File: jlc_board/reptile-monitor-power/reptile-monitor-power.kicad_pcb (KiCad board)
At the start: 4 copper layers, 38.1 x 53.3 mm, 14 parts, among them J1 AC_IN, J2 LOAD_2, J3 LOAD_1, J4 POWER CONN, K1 ALDP105W, K2 ALDP105W, U1 NUD3105DMT1G

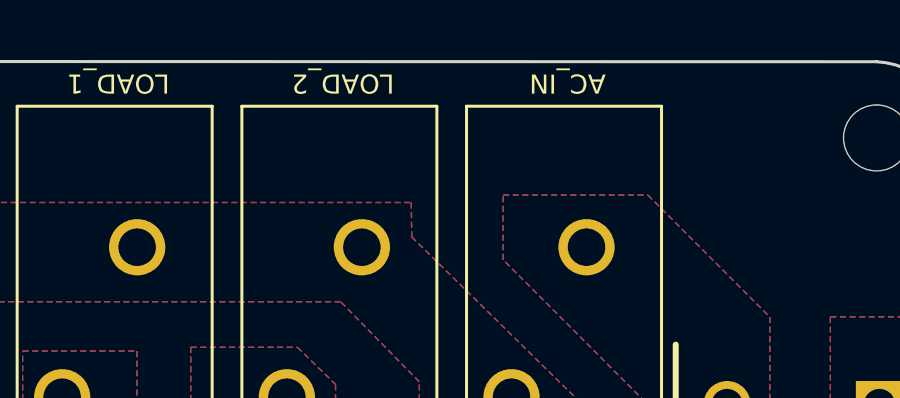
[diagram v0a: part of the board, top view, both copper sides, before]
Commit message: consolidate kicad libraries
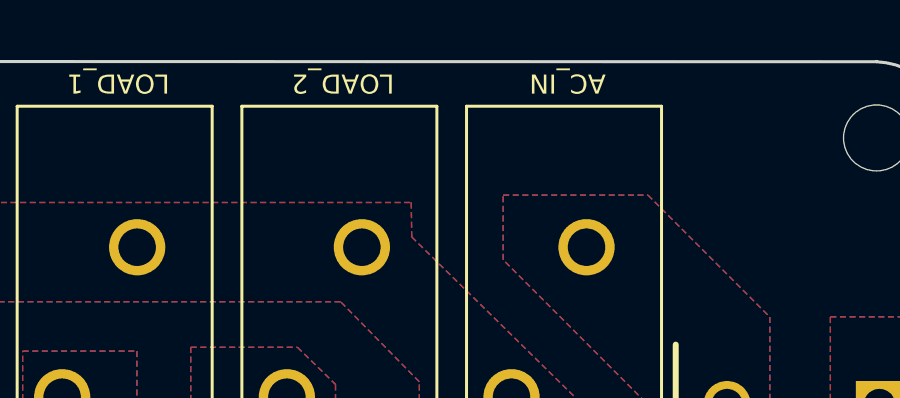
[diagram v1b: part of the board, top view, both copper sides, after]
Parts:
- F1: footprint SamacSys_Parts:TO508P400X850X850-2P -> reptile-monitor-power1:TO508P400X850X850-2P
- J1, J2, J3: footprint SamacSys_Parts:128340212 -> reptile-monitor-power1:TE Connectivity PC Terminal Block 128340212
- J4: footprint Connector_PinHeader_2.54mm:PinHeader_1x04_P2.54mm_Vertical -> reptile-monitor-power1:PinHeader_1x04_P2.54mm_Vertical
- PS1: footprint Converter_ACDC:Converter_ACDC_HiLink_HLK-PMxx -> reptile-monitor-power1:Converter_ACDC_HiLink_HLK-PMxx
- RV1: footprint Varistor:RV_Disc_D7mm_W3.4mm_P5mm -> reptile-monitor-power1:RV_Disc_D7mm_W3.4mm_P5mm
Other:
- board text added: "Rev. 3, July 2021"
- board text removed: "Rev. 3 June 2021"

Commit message: rev4
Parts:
- added REF**: WAFFLE, reptile-monitor:LOGO, B.Cu at (152.7, 83.9)
- J1, J2, J3: footprint reptile-monitor-power1:TE Connectivity PC Terminal Block 128340212 -> reptile-monitor-power:TE Connectivity PC Terminal Block 128340212
- RV1: footprint reptile-monitor-power1:RV_Disc_D7mm_W3.4mm_P5mm -> reptile-monitor-power:RV_Disc_D7mm_W3.4mm_P5mm
- moved F1 4.90 mm to (158.3, 59.9), turned to 90 degrees
- moved J1 2.60 mm to (152.9, 54.4)
- moved K1 2.60 mm to (137.5, 81.8)
- moved K2 2.60 mm to (129.2, 81.8)
- moved PS1 2.60 mm to (156.9, 64.5)
- moved J2 2.60 mm to (145.4, 54.4)
- moved J3 2.60 mm to (137.9, 54.4)
- moved RV1 1.84 mm to (132.3, 55.7)
- moved U1 1.40 mm to (138.8, 89.2)
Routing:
- net L1: track 22.2 -> 23.8 mm
- net RLY2: track 6.62 -> 8.09 mm
- net L2: track 23.9 -> 25.1 mm
- net RLY1: track 9.13 -> 10.3 mm
- net GND: track 1.97 -> 3.09 mm
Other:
- rule pad_to_mask_clearance: 0.0508 -> 0
- board text added: "+5V"
- board text added: "GND"
- board text added: "L1"
- board text added: "L2"
- board text added: "Rev. 4, Aug 2021"
- board text removed: "Rev. 3, July 2021"

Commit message: updates
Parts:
- F1: footprint reptile-monitor-power1:TO508P400X850X850-2P -> reptile-monitor-power:TO508P400X850X850-2P
- J4: footprint reptile-monitor-power1:PinHeader_1x04_P2.54mm_Vertical -> reptile-monitor-power:PinHeader_1x04_P2.54mm_Vertical
- PS1: footprint reptile-monitor-power1:Converter_ACDC_HiLink_HLK-PMxx -> reptile-monitor-power:Converter_ACDC_HiLink_HLK-PMxx
- moved REF1 58.5 mm to (129.4, 101.6), turned to 180 degrees
- moved REF1 58.5 mm to (129.4, 53.3), turned to 0 degrees
- moved REF1 58.4 mm to (162.5, 101.6), turned to 180 degrees
- moved REF1 58.4 mm to (162.5, 53.3), turned to 0 degrees
- moved RV1 51.5 mm to (159.7, 99.3), turned to 90 degrees
- moved J3 48.9 mm to (154.1, 100.6), turned to 0 degrees
- moved J4 48.9 mm to (139.5, 53.8)
- moved J1 48.2 mm to (139.1, 100.6), turned to 0 degrees
- moved J2 46.2 mm to (146.6, 100.6), turned to 0 degrees
- moved F1 42.8 mm to (133.7, 95.0), turned to -90 degrees
- moved K2 34.6 mm to (162.8, 73.2), turned to -90 degrees
- moved PS1 34.0 mm to (135.1, 90.5), turned to 90 degrees
- moved U1 27.5 mm to (153.2, 65.8), turned to 180 degrees
- moved K1 19.1 mm to (154.5, 73.2), turned to -90 degrees
- moved REF** 18.4 mm to (139.5, 71.1), turned to -90 degrees
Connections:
- J4 pad 1: +5V -> GND
- J4 pad 2: GND -> +5V
- J4 pad 3: L2 -> L1
- J4 pad 4: L1 -> L2
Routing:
- net L2: track 25.1 -> 16.6 mm
- net L1: track 23.8 -> 16.1 mm

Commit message: tt-relay
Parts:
- moved U1 6.17 mm to (155.5, 60.1), turned to 90 degrees
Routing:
- net RLY2: track 8.09 -> 18.0 mm
- net RLY1: track 10.3 -> 13.2 mm
- net L1: track 16.1 -> 13.7 mm
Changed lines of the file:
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@@
   )
   (footprint "reptile-monitor-power:ON_Semi-318F-0-0-0" (layer "F.Cu")
-    (at 153.2382 65.786 180)
+    (at 155.5242 60.0525 90)
     (property "Current - Output (Max)" "300mA")
     (property "Sheetfile" "reptile-monitor-power.kicad_sch")
@@
     (property "temperature range low" "-40°C")
     (property "voltage" "6V")
-    (fp_text reference "U1" (at -1.65 -2.4) (layer "F.SilkS") hide
-      (effects (font (size 1 1) (thickness 0.15)) (justify right))
+    (fp_text reference "U1" (at -1.65 -2.4 90) (layer "F.SilkS") hide
+      (effects (font (size 1 1) (thickness 0.15)) (justify left))
     )
-    (fp_text value "NUD3105DMT1G" (at 0 0) (layer "F.SilkS") hide
+    (fp_text value "NUD3105DMT1G" (at 0 0 90) (layer "F.SilkS") hide
       (effects (font (size 1.27 1.27) (thickness 0.15)))
     )
@@
     (fp_line (start -0.75 1.5) (end -0.75 -1.5) (layer "F.Fab") (width 0.15))
     (fp_line (start -0.75 -1.5) (end 0.75 -1.5) (layer "F.Fab") (width 0.15))
-    (pad "1" smd rect (at -1.2 -0.95 180) (size 1 0.7) (layers "F.Cu" "F.Paste" "F.Mask")
+    (pad "1" smd rect (at -1.2 -0.95 90) (size 1 0.7) (layers "F.Cu" "F.Paste" "F.Mask")
       (net 7 "GND") (pinfunction "1_Source") (pintype "unspecified"))
-    (pad "2" smd rect (at -1.2 0 180) (size 1 0.7) (layers "F.Cu" "F.Paste" "F.Mask")
+    (pad "2" smd rect (at -1.2 0 90) (size 1 0.7) (layers "F.Cu" "F.Paste" "F.Mask")
       (net 5 "L2") (pinfunction "1_Gate") (pintype "unspecified"))
-    (pad "3" smd rect (at -1.2 0.95 180) (size 1 0.7) (layers "F.Cu" "F.Paste" "F.Mask")
+    (pad "3" smd rect (at -1.2 0.95 90) (size 1 0.7) (layers "F.Cu" "F.Paste" "F.Mask")
       (net 2 "RLY1") (pinfunction "2_Drain") (pintype "unspecified"))
-    (pad "4" smd rect (at 1.2 0.95 180) (size 1 0.7) (layers "F.Cu" "F.Paste" "F.Mask")
+    (pad "4" smd rect (at 1.2 0.95 90) (size 1 0.7) (layers "F.Cu" "F.Paste" "F.Mask")
       (net 7 "GND") (pinfunction "2_Source") (pintype "unspecified"))
-    (pad "5" smd rect (at 1.2 0 180) (size 1 0.7) (layers "F.Cu" "F.Paste" "F.Mask")
+    (pad "5" smd rect (at 1.2 0 90) (size 1 0.7) (layers "F.Cu" "F.Paste" "F.Mask")
       (net 6 "L1") (pinfunction "2_Gate") (pintype "unspecified"))
-    (pad "6" smd rect (at 1.2 -0.95 180) (size 1 0.7) (layers "F.Cu" "F.Paste" "F.Mask")
+    (pad "6" smd rect (at 1.2 -0.95 90) (size 1 0.7) (layers "F.Cu" "F.Paste" "F.Mask")
       (net 1 "RLY2") (pinfunction "1_Drain") (pintype "unspecified"))
     (model "${KIPRJMOD}/reptile-monitor-power.3dshapes/SC-74-6.step"
@@
     (style (thickness 0.0254) (arrow_length 0.635) (text_position_mode 0) (extension_height 0.58642) (extension_offset 0.127) keep_text_aligned)
   )
-  (segment (start 150.7642 66.736) (end 149.801417 67.698783) (width 0.508) (layer "F.Cu") (net 1))
-  (segment (start 152.0382 66.736) (end 150.7642 66.736) (width 0.508) (layer "F.Cu") (net 1))
-  (segment (start 149.801417 67.698783) (end 149.801417 73.152) (width 0.508) (layer "F.Cu") (net 1))
-  (segment (start 158.076396 67.720196) (end 158.076396 73.151995) (width 0.508) (layer "F.Cu") (net 2))
-  (segment (start 155.1922 64.836) (end 158.076396 67.720196) (width 0.508) (layer "F.Cu") (net 2))
-  (segment (start 154.4382 64.836) (end 155.1922 64.836) (width 0.508) (layer "F.Cu") (net 2))
-  (segment (start 149.1742 53.848) (end 153.2382 57.912) (width 0.254) (layer "F.Cu") (net 5))
-  (segment (start 147.1522 53.848) (end 149.1742 53.848) (width 0.254) (layer "F.Cu") (net 5))
-  (segment (start 153.2382 65.34) (end 153.6842 65.786) (width 0.254) (layer "F.Cu") (net 5))
-  (segment (start 153.6842 65.786) (end 154.4382 65.786) (width 0.254) (layer "F.Cu") (net 5))
-  (segment (start 153.2382 57.912) (end 153.2382 65.34) (width 0.254) (layer "F.Cu") (net 5))
-  (segment (start 150.1902 65.786) (end 152.0382 65.786) (width 0.254) (layer "F.Cu") (net 6))
-  (segment (start 149.3012 64.897) (end 150.1902 65.786) (width 0.254) (layer "F.Cu") (net 6))
-  (segment (start 144.6122 53.848) (end 149.3012 58.537) (width 0.254) (layer "F.Cu") (net 6))
-  (segment (start 149.3012 58.537) (end 149.3012 64.897) (width 0.254) (layer "F.Cu") (net 6))
-  (segment (start 155.5242 67.31) (end 154.9502 66.736) (width 0.508) (layer "F.Cu") (net 7))
-  (segment (start 154.9502 66.736) (end 154.4382 66.736) (width 0.508) (layer "F.Cu") (net 7))
-  (segment (start 150.6982 64.77) (end 150.7642 64.836) (width 0.508) (layer "F.Cu") (net 7))
-  (segment (start 150.7642 64.836) (end 152.0382 64.836) (width 0.508) (layer "F.Cu") (net 7))
-  (via (at 155.5242 67.31) (size 0.762) (drill 0.4572) (layers "F.Cu" "B.Cu") (net 7))
-  (via (at 150.6982 64.77) (size 0.762) (drill 0.4572) (layers "F.Cu" "B.Cu") (net 7))
-  (zone (net 11) (net_name "+5V") (layer "F.Cu") (hatch edge 0.508)
+  (segment (start 149.801417 60.713783) (end 149.801417 73.152) (width 0.254) (layer "F.Cu") (net 1))
+  (segment (start 154.5742 58.8525) (end 151.6627 58.8525) (width 0.254) (layer "F.Cu") (net 1))
+  (segment (start 151.6627 58.8525) (end 149.801417 60.713783) (width 0.254) (layer "F.Cu") (net 1))
+  (segment (start 158.1912 62.103) (end 158.1912 73.037191) (width 0.254) (layer "F.Cu") (net 2))
+  (segment (start 156.4742 61.2525) (end 157.3407 61.2525) (width 0.254) (layer "F.Cu") (net 2))
+  (segment (start 158.1912 73.037191) (end 158.076396 73.151995) (width 0.254) (layer "F.Cu") (net 2))
+  (segment (start 157.3407 61.2525) (end 158.1912 62.103) (width 0.254) (layer "F.Cu") (net 2))
+  (segment (start 147.1014 53.848) (end 148.3714 55.118) (width 0.254) (layer "F.Cu") (net 5))
+  (segment (start 157.4292 57.541902) (end 157.4292 59.563) (width 0.254) (layer "F.Cu") (net 5))
+  (segment (start 155.5242 60.693078) (end 155.5242 61.2525) (width 0.254) (layer "F.Cu") (net 5))
+  (segment (start 157.4292 59.563) (end 156.9212 60.071) (width 0.254) (layer "F.Cu") (net 5))
+  (segment (start 148.3714 55.118) (end 155.005298 55.118) (width 0.254) (layer "F.Cu") (net 5))
+  (segment (start 156.146278 60.071) (end 155.5242 60.693078) (width 0.254) (layer "F.Cu") (net 5))
+  (segment (start 155.005298 55.118) (end 157.4292 57.541902) (width 0.254) (layer "F.Cu") (net 5))
+  (segment (start 156.9212 60.071) (end 156.146278 60.071) (width 0.254) (layer "F.Cu") (net 5))
+  (segment (start 144.5614 53.848) (end 146.9744 56.261) (width 0.254) (layer "F.Cu") (net 6))
+  (segment (start 155.5242 57.785) (end 155.5242 58.8525) (width 0.254) (layer "F.Cu") (net 6))
+  (segment (start 146.9744 56.261) (end 154.0002 56.261) (width 0.254) (layer "F.Cu") (net 6))
+  (segment (start 154.0002 56.261) (end 155.5242 57.785) (width 0.254) (layer "F.Cu") (net 6))
+  (segment (start 156.2862 57.531) (end 156.4742 57.719) (width 0.254) (layer "F.Cu") (net 7))
+  (segment (start 156.4742 57.719) (end 156.4742 58.8525) (width 0.254) (layer "F.Cu") (net 7))
+  (segment (start 153.4922 60.1705) (end 154.5742 61.2525) (width 0.254) (layer "F.Cu") (net 7))
+  (segment (start 153.4922 60.071) (end 153.4922 60.1705) (width 0.254) (layer "F.Cu") (net 7))
+  (via (at 156.2862 57.531) (size 0.762) (drill 0.4572) (layers "F.Cu" "B.Cu") (net 7))
+  (via (at 153.4922 60.071) (size 0.762) (drill 0.4572) (layers "F.Cu" "B.Cu") (net 7))
+  (zone locked (net 11) (net_name "+5V") (layer "F.Cu") (hatch edge 0.508)
     (connect_pads yes (clearance 0.508))
     (min_thickness 0.254) (filled_areas_thickness no)
